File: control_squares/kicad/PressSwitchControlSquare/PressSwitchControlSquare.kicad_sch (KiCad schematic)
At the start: 6 parts, among them J1 Battery, J2 LED_NEOPIXEL, J3 Batt_switch, J4 QMC5833, J5 Trigger_Sw, U1 ESP32-C3_SUPERMINI_SMD

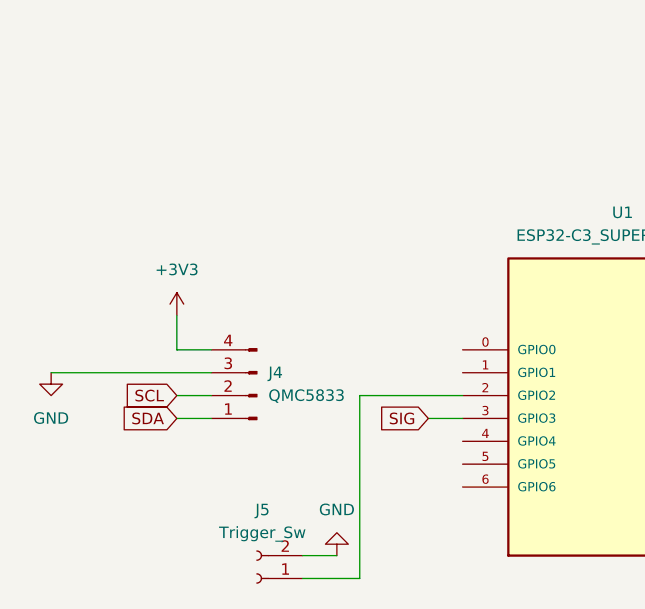
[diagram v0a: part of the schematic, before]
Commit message: added another pin to trigger
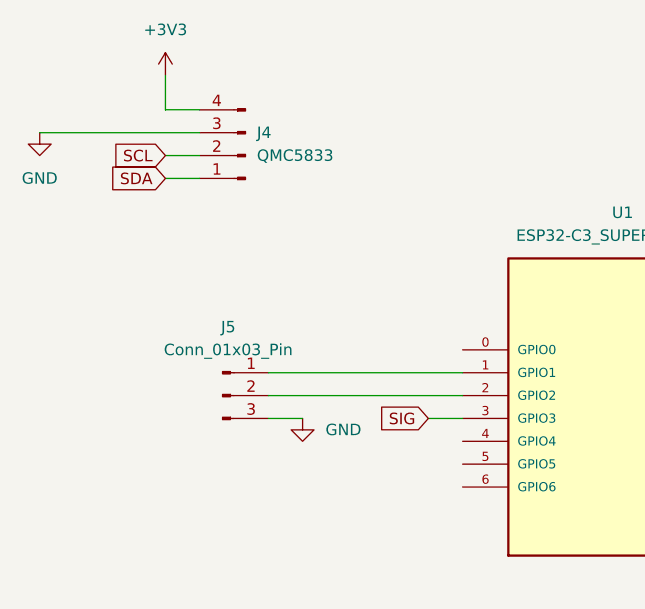
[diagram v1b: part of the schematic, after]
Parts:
- removed J5: Trigger_Sw, Connector_JST:JST_PH_B2B-PH-SM4-TB_1x02-1MP_P2.00mm_Vertical, symbol Connector:Conn_01x02_Socket
- added J5: Conn_01x03_Pin, Connector_JST:JST_PH_B3B-PH-SM4-TB_1x03-1MP_P2.00mm_Vertical, symbol Connector:Conn_01x03_Pin
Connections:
- net GND: now also J5.3 (Pin_3)
- net at U1.1 (GPIO1): now also J5.1 (Pin_1)
- net at U1.2 (GPIO2): now also J5.2 (Pin_2)
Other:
- moved on the sheet: J4

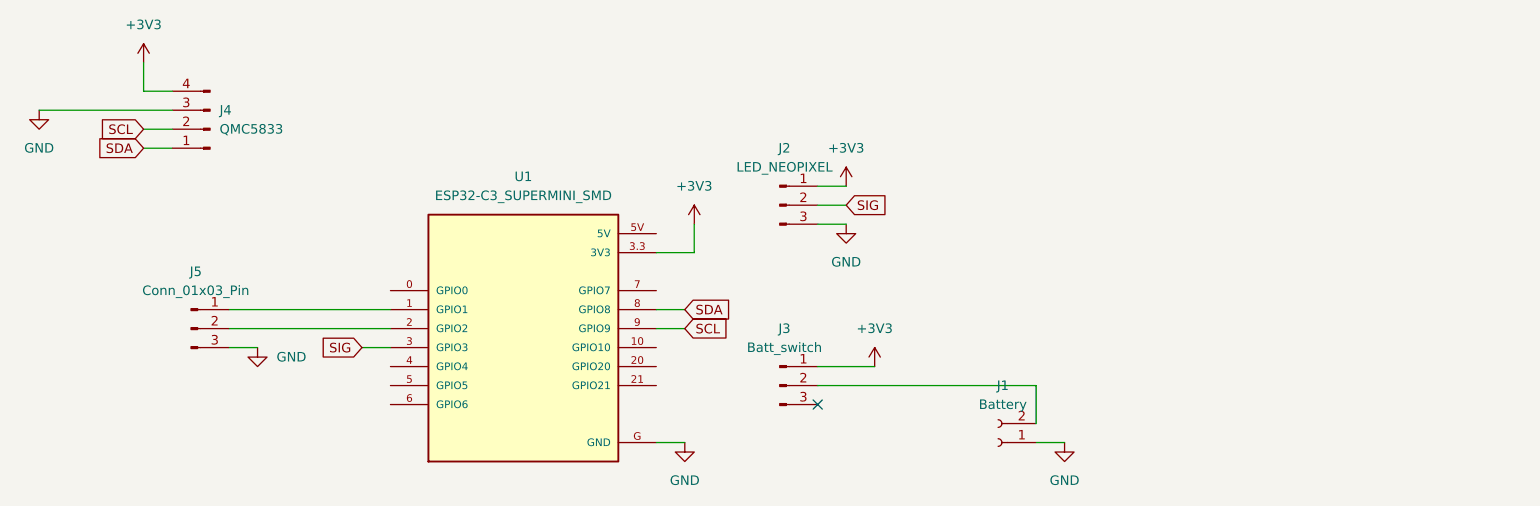
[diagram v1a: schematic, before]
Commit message: added voltage regulator
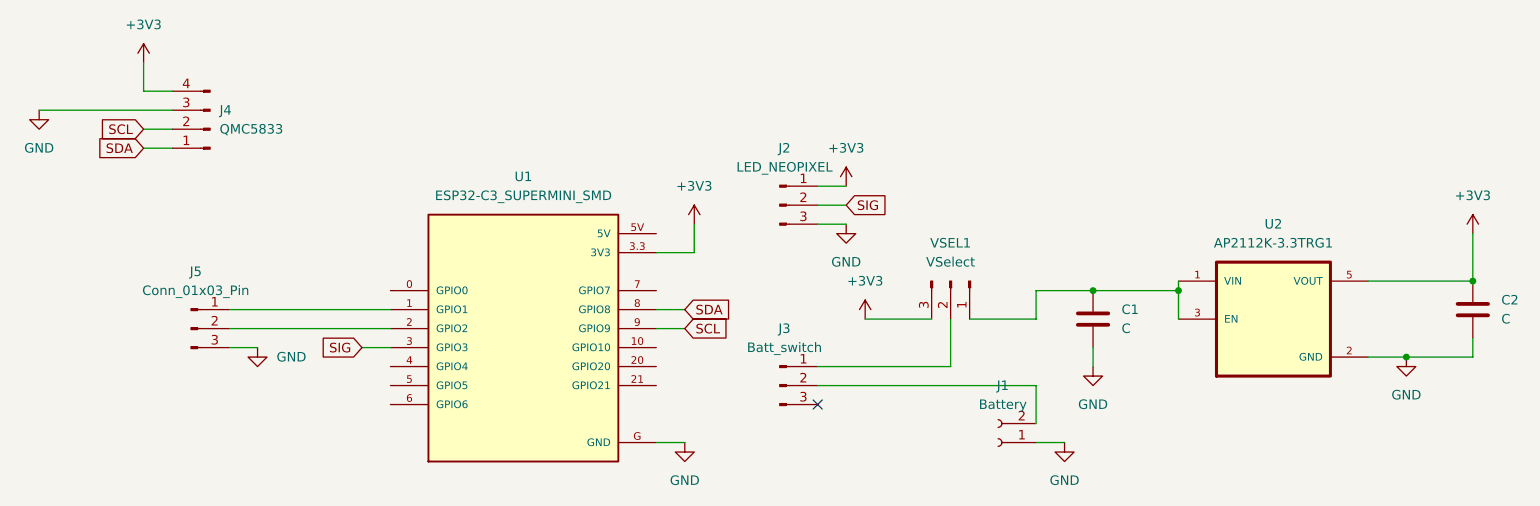
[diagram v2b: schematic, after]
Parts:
- added C1, C2: C, Capacitor_SMD:C_0603_1608Metric, symbol Device:C
- added U2: AP2112K-3.3TRG1, AP2112K-3.3TRG1:SOT95P285X140-5N, symbol AP2112K-3.3TRG1:AP2112K-3.3TRG1
- added VSEL1: VSelect, Connector_PinHeader_2.54mm:PinHeader_1x03_P2.54mm_Vertical, symbol Connector:Conn_01x03_Pin
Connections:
- net +3V3: now also C2.1, U2.5 (VOUT), VSEL1.3 (Pin_3); no longer J3.1 (Pin_1)
- net GND: now also C1.2, C2.2, U2.2 (GND)
- new net: J3.1 (Pin_1), VSEL1.2 (Pin_2)
- new net: C1.1, U2.1 (VIN), U2.3 (EN), VSEL1.1 (Pin_1)

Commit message: fixed mirroring
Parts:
- added J6: Conn_01x04_Pin, symbol Connector:Conn_01x04_Pin
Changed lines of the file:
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@@
+	)
+	(symbol
+		(lib_id "Connector:Conn_01x04_Pin")
+		(at 57.15 96.52 0)
+		(unit 1)
+		(exclude_from_sim no)
+		(in_bom yes)
+		(on_board yes)
+		(dnp no)
+		(fields_autoplaced yes)
+		(property "Reference" "J6"
+			(at 57.785 88.9 0)
+			(effects
+				(font
+					(size 1.27 1.27)
+				)
+			)
+		)
+		(property "Value" "Conn_01x04_Pin"
+			(at 57.785 91.44 0)
+			(effects
+				(font
+					(size 1.27 1.27)
+				)
+			)
+		)
+		(property "Footprint" ""
+			(at 57.15 96.52 0)
+			(effects
+				(font
+					(size 1.27 1.27)
+				)
+				(hide yes)
+			)
+		)
+		(property "Datasheet" "~"
+			(at 57.15 96.52 0)
+			(effects
+				(font
+					(size 1.27 1.27)
+				)
+				(hide yes)
+			)
+		)
+		(property "Description" "Generic connector, single row, 01x04, script generated"
+			(at 57.15 96.52 0)
+			(effects
+				(font
+					(size 1.27 1.27)
+				)
+				(hide yes)
+			)
+		)
+		(pin "4"
+		)
+		(pin "2"
+		)
+		(pin "3"
+		)
+		(pin "1"
+		)
+		(instances
+			(project ""
+				(path "/a65a7e5b-df7b-4680-bd24-007c253c9cc6"
+					(reference "J6")
+					(unit 1)
+				)
+			)
+		)
 	)
 	(symbol
